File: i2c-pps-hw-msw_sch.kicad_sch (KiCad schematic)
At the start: 12 parts, among them J1 +5V, Q5 SiA449DJ, Q6 MMBT3904

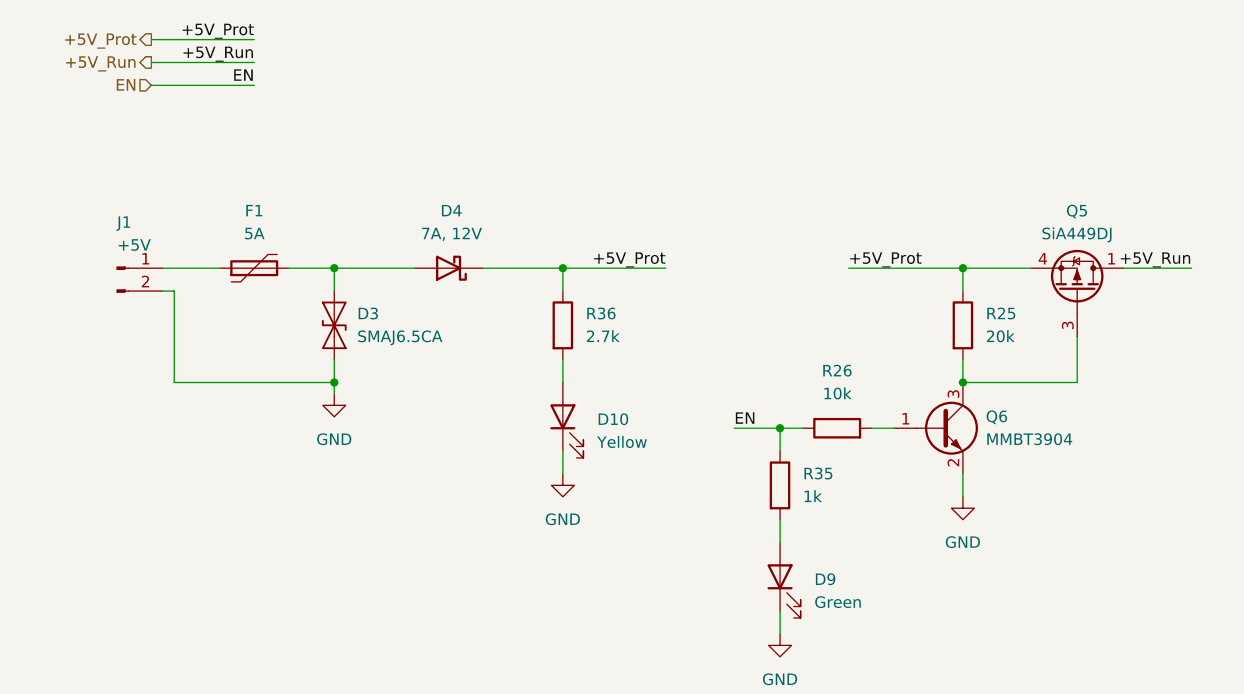
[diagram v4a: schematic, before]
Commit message: Switch to MOSFET based polarity protection
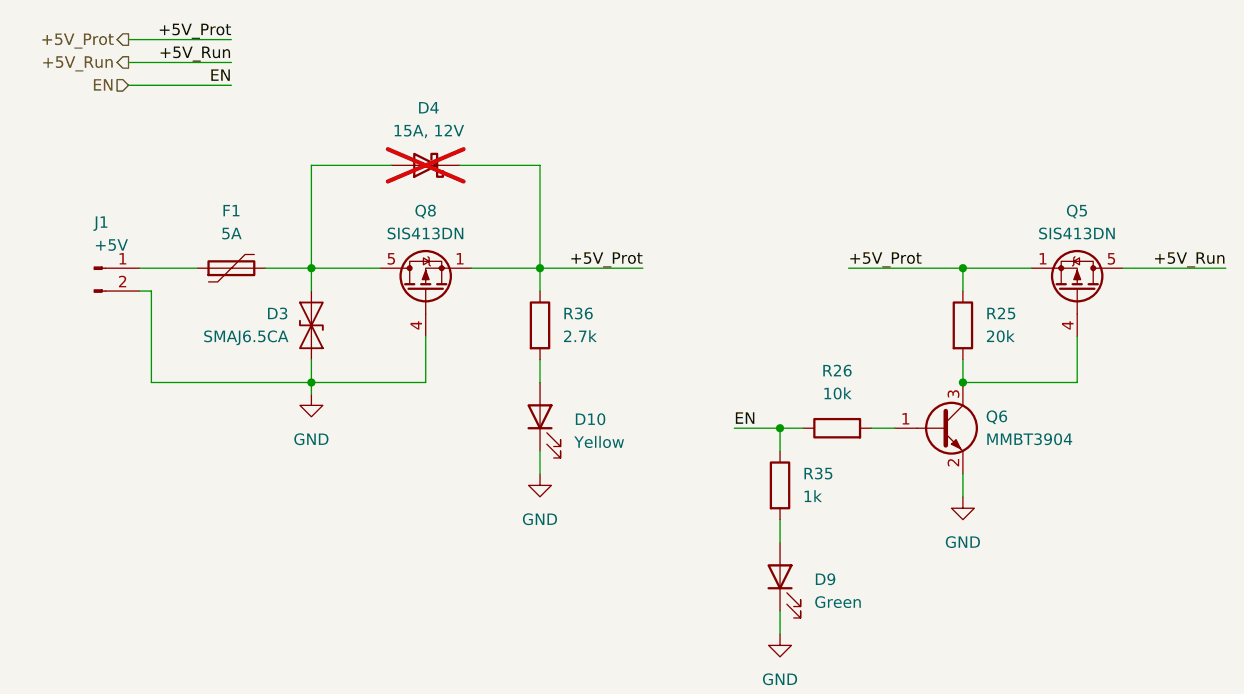
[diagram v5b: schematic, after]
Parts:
- added Q8: SIS413DN, Package_SO:Vishay_PowerPAK_1212-8_Single, symbol Transistor_FET:SiS415DNT
- D4: value 7A, 12V -> 15A, 12V; now not fitted
- Q5: value SiA449DJ -> SIS413DN; footprint Package_TO_SOT_SMD:Vishay_PowerPAK_SC70-6L_Single -> Package_SO:Vishay_PowerPAK_1212-8_Single; symbol Transistor_FET:SiA449DJ -> Transistor_FET:SiS415DNT
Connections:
- net +5V_Prot: now also Q5.1 (S), Q5.2 (S), Q5.3 (S), Q8.1 (S), Q8.2 (S), Q8.3 (S); no longer Q5.4 (S)
- net +5V_Run: now also Q5.5 (D); no longer Q5.1 (D)
- net GND: now also Q8.4 (G)
- net at D3.2 (A2), D4.2 (A), F1.2: now also Q8.5 (D)
- net at Q6.3 (C), R25.2: now also Q5.4 (G); no longer Q5.3 (G)
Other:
- moved on the sheet: D10, D3, F1, J1, R36

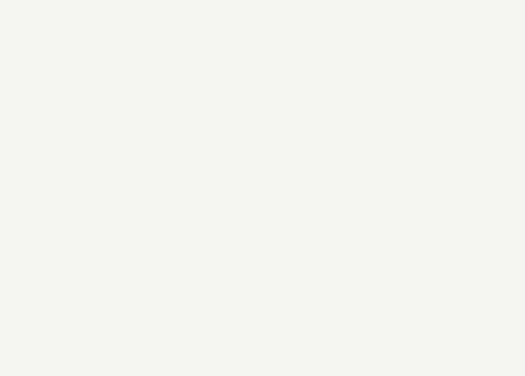
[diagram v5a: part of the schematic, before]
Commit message: Fix errors and warnings reported by ERC
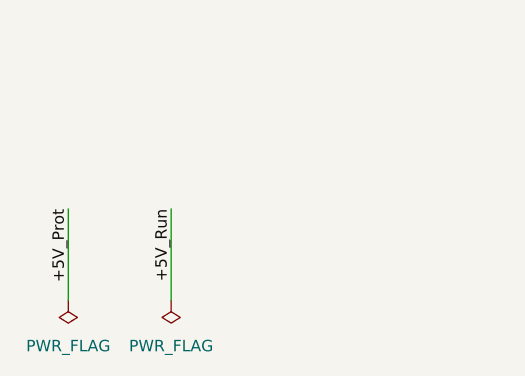
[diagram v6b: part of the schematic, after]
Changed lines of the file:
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@@
+	(wire
+		(pts
+			(xy 17.78 186.69) (xy 17.78 196.85)
+		)
+		(stroke
+			(width 0)
+			(type default)
+		)
+	)
 	(wire
 		(pts
@@
 	(wire
 		(pts
+			(xy 29.21 186.69) (xy 29.21 196.85)
+		)
+		(stroke
+			(width 0)
+			(type default)
+		)
+	)
+	(wire
+		(pts
 			(xy 105.41 90.17) (xy 114.3 90.17)
 		)
@@
 			(width 0)
 			(type default)
+		)
+	)
+	(label "+5V_Prot"
+		(at 17.78 186.69 270)
+		(effects
+			(font
+				(size 1.27 1.27)
+			)
+			(justify right bottom)
 		)
 	)
@@
 	(label "+5V_Prot"
 		(at 96.52 76.2 180)
+		(effects
+			(font
+				(size 1.27 1.27)
+			)
+			(justify right bottom)
+		)
+	)
+	(label "+5V_Run"
+		(at 29.21 186.69 270)
 		(effects
 			(font
@@
 	)
 	(symbol
+		(lib_id "power:PWR_FLAG")
+		(at 29.21 196.85 180)
+		(unit 1)
+		(exclude_from_sim no)
+		(in_bom yes)
+		(on_board yes)
+		(dnp no)
+		(fields_autoplaced yes)
+		(property "Reference" "#FLG02"
+			(at 29.21 198.755 0)
+			(effects
+				(font
+					(size 1.27 1.27)
+				)
+				(hide yes)
+			)
+		)
+		(property "Value" "PWR_FLAG"
+			(at 29.21 201.93 0)
+			(effects
+				(font
+					(size 1.27 1.27)
+				)
+			)
+		)
+		(property "Footprint" ""
+			(at 29.21 196.85 0)
+			(effects
+				(font
+					(size 1.27 1.27)
+				)
+				(hide yes)
+			)
+		)
+		(property "Datasheet" "~"
+			(at 29.21 196.85 0)
+			(effects
+				(font
+					(size 1.27 1.27)
+				)
+				(hide yes)
+			)
+		)
+		(property "Description" "Special symbol for telling ERC where power comes from"
+			(at 29.21 196.85 0)
+			(effects
+				(font
+					(size 1.27 1.27)
+				)
+				(hide yes)
+			)
+		)
+		(pin "1"
+		)
+		(instances
+			(project "i2c-pps-hw"
+				(path "/512c4d3f-92f6-4670-bf9b-2123d46bbde3/242a0190-1834-4b2f-bfa7-cf55bc2f9217"
+					(reference "#FLG02")
+					(unit 1)
+				)
+			)
+		)
+	)
+	(symbol
 		(lib_id "power:GND")
 		(at 130.81 124.46 0)
@@
 					(unit 1)
 				)
+			)
+		)
+	)
+	(symbol
+		(lib_id "power:PWR_FLAG")
+		(at 17.78 196.85 180)
+		(unit 1)
+		(exclude_from_sim no)
+		(in_bom yes)
+		(on_board yes)
+		(dnp no)
+		(fields_autoplaced yes)
+		(property "Reference" "#FLG01"
+			(at 17.78 198.755 0)
+			(effects
+				(font
+					(size 1.27 1.27)
+				)
+				(hide yes)
+			)
+		)
+		(property "Value" "PWR_FLAG"
+			(at 17.78 201.93 0)
+			(effects
+				(font
+					(size 1.27 1.27)
+				)
+			)
+		)
+		(property "Footprint" ""
+			(at 17.78 196.85 0)
+			(effects
+				(font
+					(size 1.27 1.27)
+				)
+				(hide yes)
+			)
+		)
+		(property "Datasheet" "~"
+			(at 17.78 196.85 0)
+			(effects
+				(font
+					(size 1.27 1.27)
+				)
+				(hide yes)
+			)
+		)
+		(property "Description" "Special symbol for telling ERC where power comes from"
+			(at 17.78 196.85 0)
+			(effects
+				(font
+					(size 1.27 1.27)
+				)
+				(hide yes)
+			)
+		)
+		(pin "1"
+		)
+		(instances
+			(project ""
+				(path "/512c4d3f-92f6-4670-bf9b-2123d46bbde3/242a0190-1834-4b2f-bfa7-cf55bc2f9217"
+					(reference "#FLG01")
+					(unit 1)
+				)
